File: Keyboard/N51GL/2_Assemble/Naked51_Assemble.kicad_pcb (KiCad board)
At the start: 2 copper layers, 305.8 x 99.2 mm, 124 parts, among them J1 Conn_01x02, SW1 SW_PUSH, SW10 SW_PUSH, SW11 SW_PUSH, SW12 SW_PUSH, SW13 SW_PUSH, SW14 SW_PUSH, SW15 SW_PUSH, SW16 SW_PUSH, SW17 SW_PUSH, SW18 SW_PUSH, SW19 SW_PUSH, SW2 Rotary_Encoder_Switch, SW20 SW_PUSH, SW21 SW_PUSH, SW22 SW_PUSH, SW23 SW_PUSH, SW24 SW_PUSH, SW25 SW_PUSH, SW26 SW_PUSH, SW27 SW_PUSH, SW28 SW_PUSH, SW29 SW_PUSH, SW3 SW_PUSH, SW30 SW_PUSH, SW31 SW_PUSH, SW32 SW_PUSH, SW33 SW_PUSH, SW34 SW_PUSH, SW35 SW_PUSH, SW36 SW_PUSH, SW37 SW_PUSH, SW38 SW_PUSH, SW39 SW_PUSH, SW4 SW_PUSH, SW40 SW_PUSH, SW41 SW_PUSH, SW42 SW_PUSH, SW43 SW_PUSH, SW44 SW_PUSH, SW45 SW_PUSH, SW46 SW_PUSH, SW47 SW_PUSH, SW48 SW_PUSH, SW49 SW_PUSH, SW5 SW_PUSH, SW50 SW_PUSH, SW51 SW_PUSH, SW52 SW_PUSH, SW53 SW_PUSH, SW6 SW_PUSH, SW7 SW_PUSH, SW8 SW_PUSH, SW9 SW_PUSH, U1 BLEMicroPro

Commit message: 寸法更新とか
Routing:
- net Reset: track 58.2 -> 49.3 mm
- net VCC: track 1015.9 -> 1020.5 mm
- net Col2: track 415.3 -> 414.4 mm
- net LED: track 312.3 -> 311.7 mm
- net GND: track 864.6 -> 864.1 mm
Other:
- board size 305.8 x 99.2 mm -> 304.4 x 98.8 mm

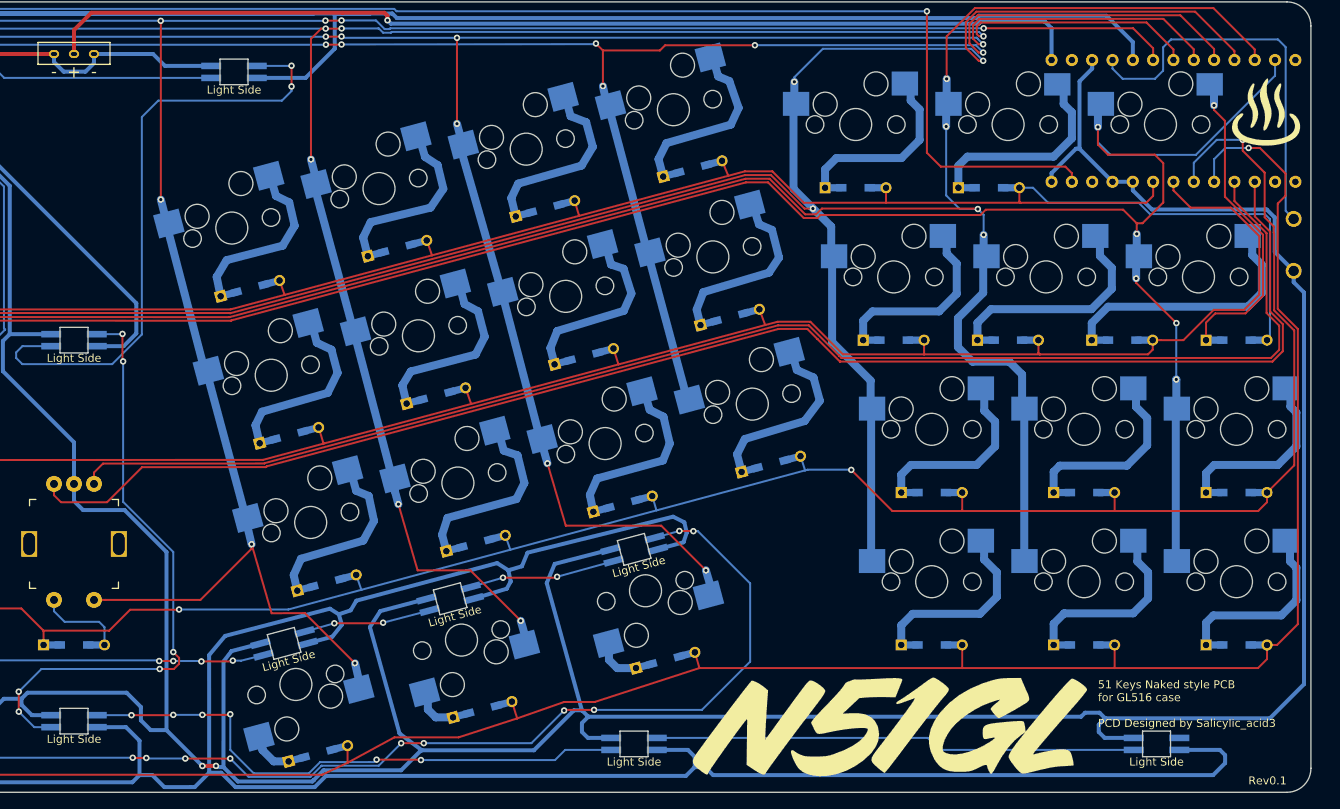
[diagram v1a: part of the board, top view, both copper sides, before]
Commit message: 電池コネクタの更新、シルクの修正
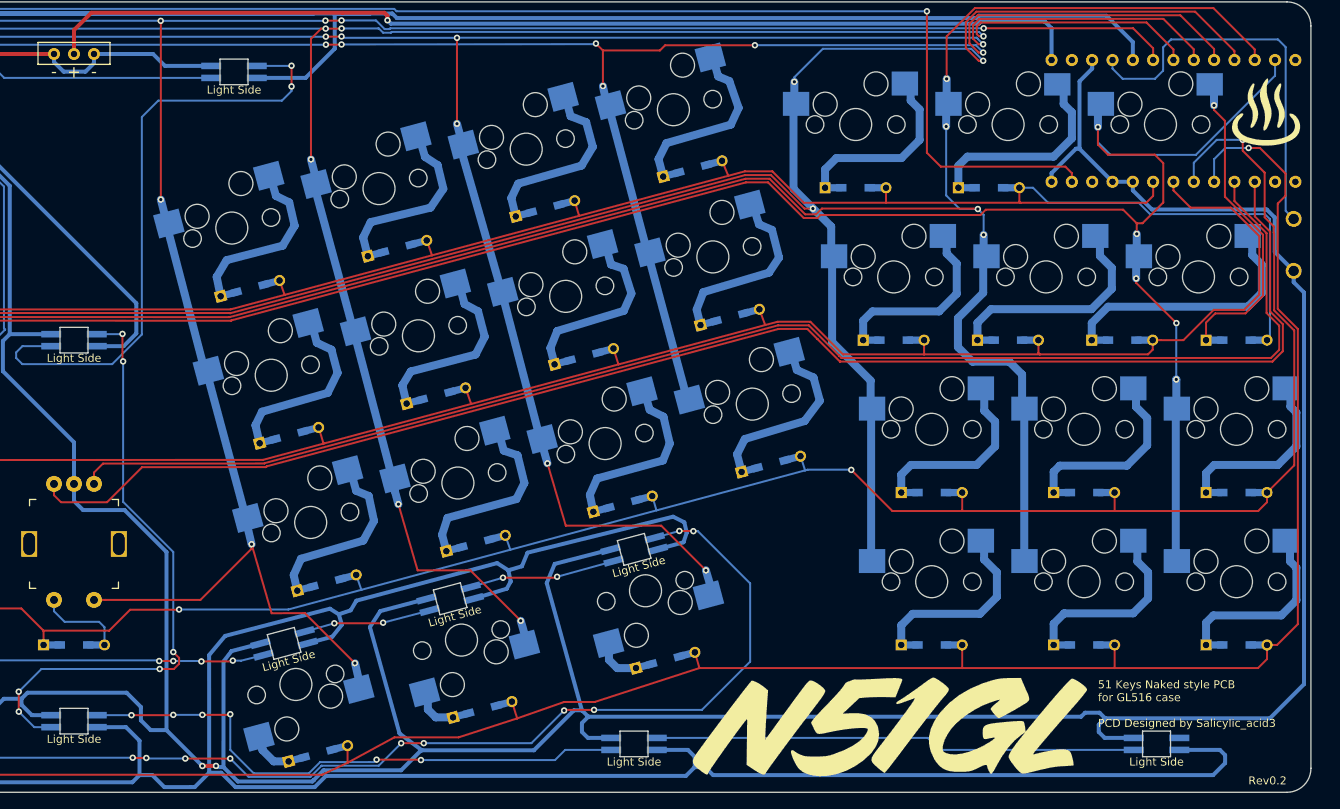
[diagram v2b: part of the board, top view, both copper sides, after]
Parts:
- J1: footprint kbd_Parts:Battery_XH2.5_GL_rev -> kbd_Parts:Battery_XH2.5_GL_PCB
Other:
- board text added: "Rev0.2"
- board text removed: "Rev0.1"
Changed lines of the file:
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@@
     (add_net VCC)
   )
-  (module kbd_Parts:Battery_XH2.5_GL_rev (layer B.Cu)
+  (module kbd_Parts:Battery_XH2.5_GL_PCB (layer B.Cu)
     (at 169.008711 23.8125)
     (fp_text reference J1 (at -3 2) (layer B.Fab)
@@
       (effects (font (size 1 1) (thickness 0.15)) (justify mirror))
     )
-    (fp_line (start -4.5 -1.5) (end -4.5 1.25) (layer F.SilkS) (width 0.15))
-    (fp_line (start -4.5 1.25) (end 4.5 1.25) (layer F.SilkS) (width 0.15))
-    (fp_line (start 4.5 -1.5) (end -4.5 -1.5) (layer F.SilkS) (width 0.15))
     (fp_line (start 4.5 1.25) (end 4.5 -1.5) (layer F.SilkS) (width 0.15))
+    (fp_line (start 4.5 -1.5) (end -4.5 -1.5) (layer F.SilkS) (width 0.15))
+    (fp_line (start -4.5 1.25) (end 4.5 1.25) (layer F.SilkS) (width 0.15))
+    (fp_line (start -4.5 -1.5) (end -4.5 1.25) (layer F.SilkS) (width 0.15))
     (fp_line (start 4.5 1.25) (end 4.5 -1.5) (layer B.SilkS) (width 0.15))
     (fp_line (start -4.5 1.25) (end 4.5 1.25) (layer B.SilkS) (width 0.15))
@@
       (effects (font (size 1 1) (thickness 0.15)) (justify mirror))
     )
-    (pad 2 thru_hole oval (at -2.5 -0.05) (size 1.3 1) (drill oval 0.8 0.5) (layers *.Cu *.Mask)
+    (pad 2 thru_hole oval (at -2.5 -0.05) (size 1.5 1.5) (drill oval 0.8) (layers *.Cu *.Mask)
       (net 1 GND) (clearance 0.15))
-    (pad 1 thru_hole oval (at 0 -0.05) (size 1.3 1) (drill oval 0.8 0.5) (layers *.Cu *.Mask)
+    (pad 1 thru_hole oval (at 0 -0.05) (size 1.5 1.5) (drill oval 0.8) (layers *.Cu *.Mask)
       (net 58 Bat+) (clearance 0.15))
-    (pad 2 thru_hole oval (at 2.5 -0.05) (size 1.3 1) (drill oval 0.8 0.5) (layers *.Cu *.Mask)
+    (pad 2 thru_hole oval (at 2.5 -0.05) (size 1.5 1.5) (drill oval 0.8) (layers *.Cu *.Mask)
       (net 1 GND) (clearance 0.15))
     (model "../../../../../../Users/pluis/Documents/Magic Briefcase/Documents/KiCad/3d/AB2_TRS_3p5MM_PTH.wrl"
@@
   (module kbd_Parts:LED_SK6812MINI-E_BL (layer B.Cu)
     (at 239.008711 110)
-    (fp_text reference L14 (at 0 -2.8) (layer B.SilkS) hide
+    (fp_text reference L14 (at 0 -2.8) (layer B.SilkS)
       (effects (font (size 1 1) (thickness 0.15)) (justify mirror))
     )
@@
   (module kbd_Parts:LED_SK6812MINI-E_BL (layer B.Cu)
     (at 38.575 110)
-    (fp_text reference L8 (at 0 -2.8) (layer B.SilkS) hide
+    (fp_text reference L8 (at 0 -2.8) (layer B.SilkS)
       (effects (font (size 1 1) (thickness 0.15)) (justify mirror))
     )
@@
     (tags R)
     (autoplace_cost180 10)
-    (fp_text reference D1 (at 0 -1.63) (layer B.SilkS)
+    (fp_text reference D1 (at 0.005 1.5475) (layer B.SilkS)
       (effects (font (size 1 1) (thickness 0.125)) (justify mirror))
     )
@@
     )
   )
-  (gr_text Rev0.1 (at 318.2 114.6) (layer F.SilkS)
+  (gr_text Rev0.2 (at 318.2 114.6) (layer F.SilkS)
     (effects (font (size 1 1) (thickness 0.15)))
   )

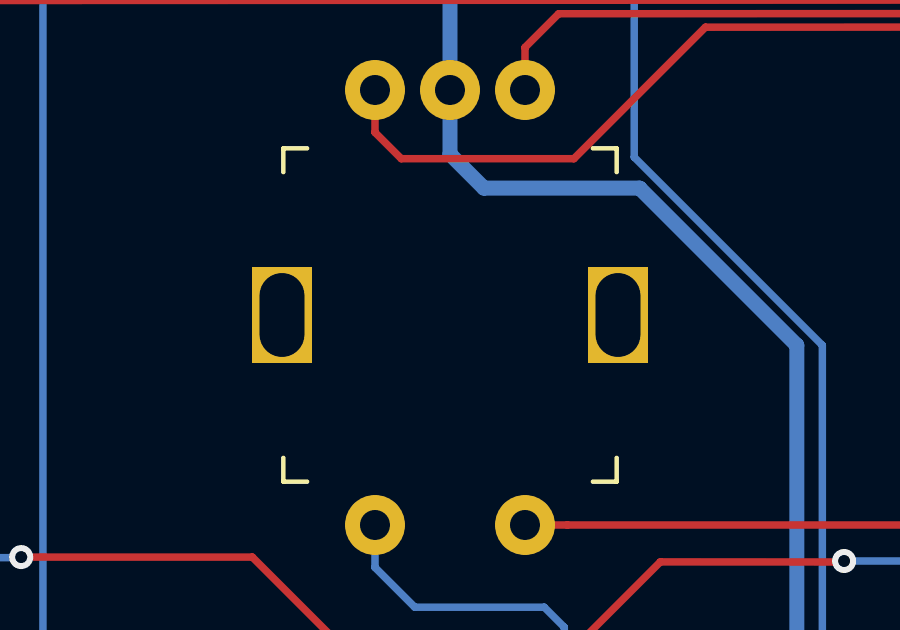
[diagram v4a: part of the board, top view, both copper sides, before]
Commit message: 使用するフットプリントを最新化
・EC12
・バッテリーピン
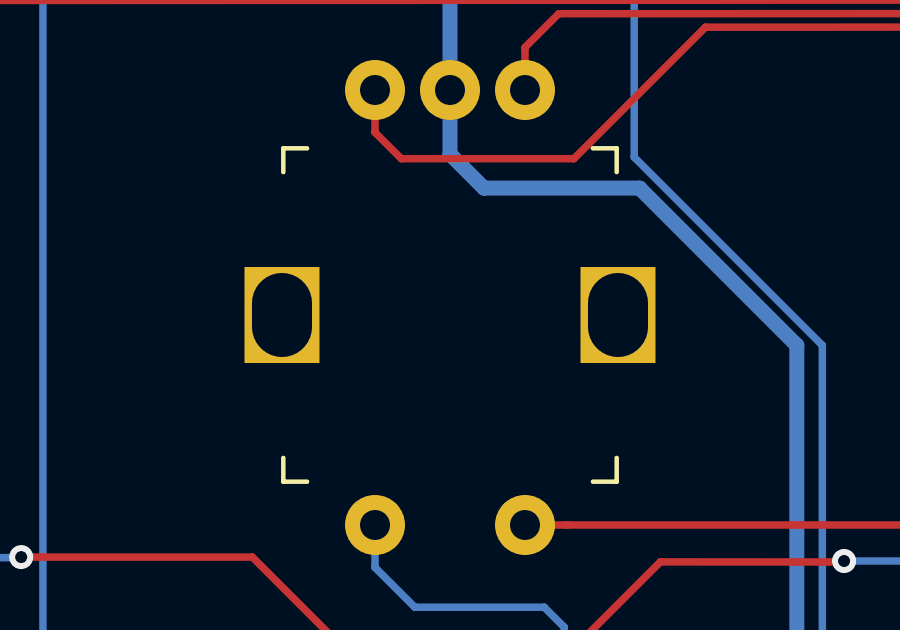
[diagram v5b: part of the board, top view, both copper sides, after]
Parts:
- SW2: footprint kbd_Parts:RotaryEncoder_EC11E -> kbd_Parts:RotaryEncoder_EC12E

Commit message: バージョン番号変更
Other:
- board text added: "Rev1.0"
- board text removed: "Rev0.2"
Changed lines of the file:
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@@
   (general
     (thickness 1.6)
-    (drawings 18)
+    (drawings 20)
     (tracks 1844)
     (zones 0)
@@
       (drillshape 0)
       (scaleselection 1)
-      (outputdirectory "../../../../../../../自作キーボード/発注/20210621/N51GL_Mid/"))
+      (outputdirectory "../../../../../自キ設計_プライベート/発注/20211222/N51M/"))
   )
   (net 0 "")
@@
       (effects (font (size 1 1) (thickness 0.15)))
     )
-    (fp_text user %R (at 3.6 3.8 90) (layer F.Fab)
-      (effects (font (size 1 1) (thickness 0.15)))
-    )
     (fp_line (start -5.55625 5.55625) (end -4.7625 5.55625) (layer F.SilkS) (width 0.15))
     (fp_line (start -5.55625 4.7625) (end -5.55625 5.55625) (layer F.SilkS) (width 0.15))
@@
     (fp_line (start -6.1 4.3) (end -6.1 5.9) (layer F.Fab) (width 0.12))
     (fp_line (start 6.1 -5.9) (end 6.1 -4.3) (layer F.Fab) (width 0.12))
+    (fp_text user %R (at 3.6 3.8 90) (layer F.Fab)
+      (effects (font (size 1 1) (thickness 0.15)))
+    )
     (pad S1 thru_hole circle (at 7 2.5 270) (size 2 2) (drill 1) (layers *.Cu *.Mask)
       (net 4 "Net-(D2-Pad2)"))
@@
     )
   )
-  (gr_text Rev0.2 (at 318.2 114.6) (layer F.SilkS)
+  (dimension 98.8 (width 0.15) (layer Dwgs.User)
+    (gr_text "98.800 mm" (at 8.225001 66.65 270) (layer Dwgs.User)
+      (effects (font (size 1 1) (thickness 0.15)))
+    )
+    (feature1 (pts (xy 22.275 116.05) (xy 8.93858 116.05)))
+    (feature2 (pts (xy 22.275 17.25) (xy 8.93858 17.25)))
+    (crossbar (pts (xy 9.525001 17.25) (xy 9.525001 116.05)))
+    (arrow1a (pts (xy 9.525001 116.05) (xy 8.93858 114.923496)))
+    (arrow1b (pts (xy 9.525001 116.05) (xy 10.111422 114.923496)))
+    (arrow2a (pts (xy 9.525001 17.25) (xy 8.93858 18.376504)))
+    (arrow2b (pts (xy 9.525001 17.25) (xy 10.111422 18.376504)))
+  )
+  (dimension 304.35 (width 0.15) (layer Dwgs.User)
+    (gr_text "304.350 mm" (at 171.45 8.225) (layer Dwgs.User)
+      (effects (font (size 1 1) (thickness 0.15)))
+    )
+    (feature1 (pts (xy 19.275 20.25) (xy 19.275 8.938579)))
+    (feature2 (pts (xy 323.625 20.25) (xy 323.625 8.938579)))
+    (crossbar (pts (xy 323.625 9.525) (xy 19.275 9.525)))
+    (arrow1a (pts (xy 19.275 9.525) (xy 20.401504 8.938579)))
+    (arrow1b (pts (xy 19.275 9.525) (xy 20.401504 10.111421)))
+    (arrow2a (pts (xy 323.625 9.525) (xy 322.498496 8.938579)))
+    (arrow2b (pts (xy 323.625 9.525) (xy 322.498496 10.111421)))
+  )
+  (gr_text Rev1.0 (at 318.2 114.6) (layer F.SilkS)
     (effects (font (size 1 1) (thickness 0.15)))
   )

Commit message: フットプリント名の変更に対応
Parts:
- SW1, SW11, SW12, SW13, SW14, SW15, SW16, SW18, SW19, SW20, SW22, SW23, SW24, SW25, SW26, SW27, SW28, SW29, SW3, SW30, SW31, SW32, SW34, SW35, SW36, SW38, SW39, SW40, SW41, SW42, SW43, SW44, SW46, SW47, SW48, SW50, SW51, SW52, SW7, SW8, SW9: footprint kbd_SW:CherryMX_Hotswap_1.0u -> kbd_SW:CherryMX_Hotswap_1u
- SW45, SW49: footprint kbd_SW:CherryMX_Hotswap_1.0u_Small1 -> kbd_SW:CherryMX_Hotswap_1u_Small1
